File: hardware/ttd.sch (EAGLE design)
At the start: 12 parts, among them Q1 IRF540, Q2 IRF540, Q3 IRF540, Q4 IRF540

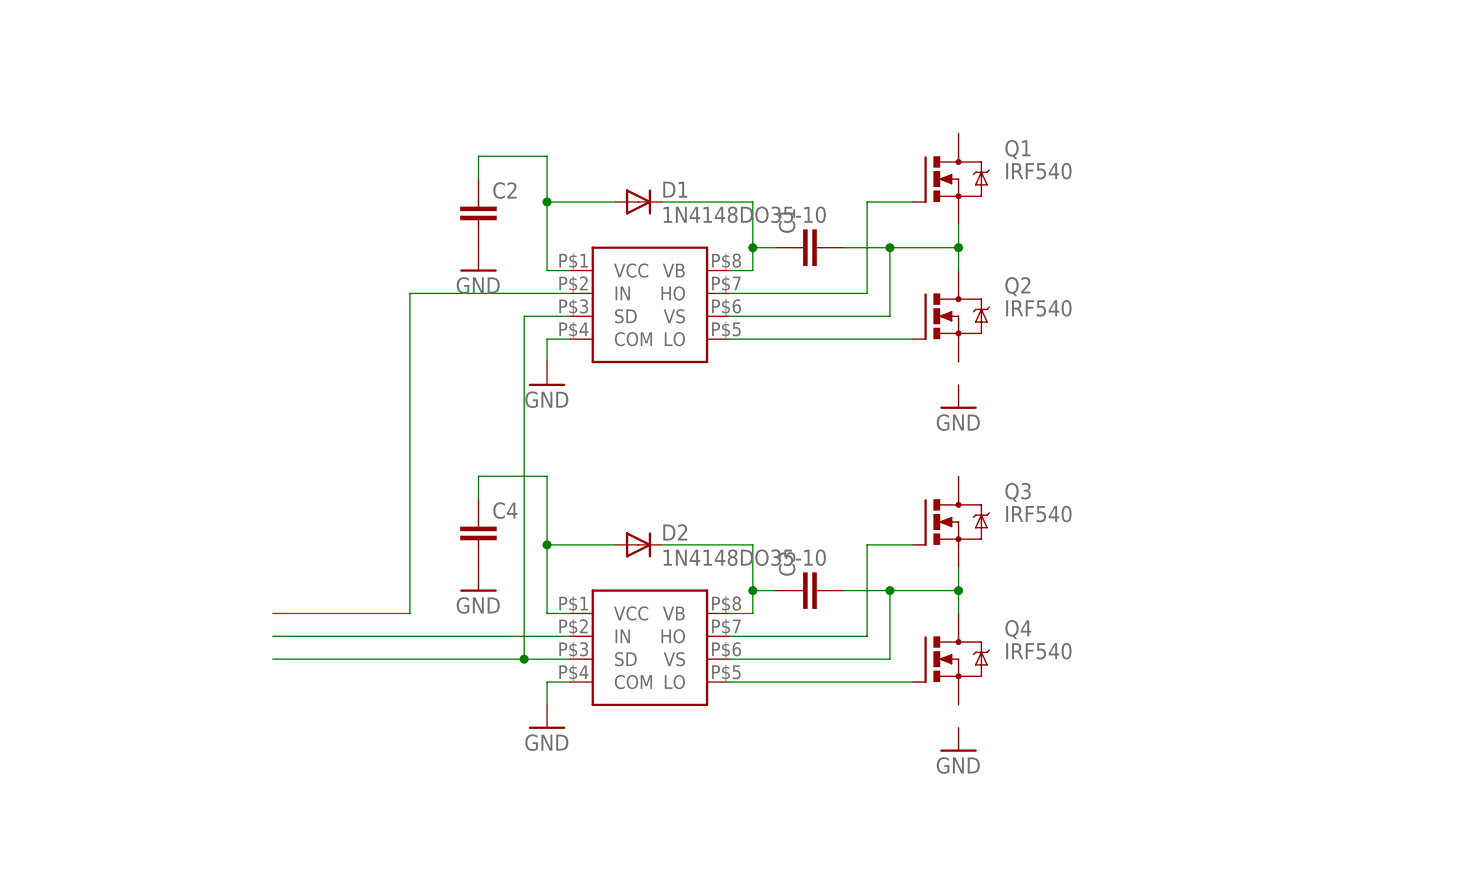
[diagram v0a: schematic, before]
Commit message: Schottkydioden eingefügt
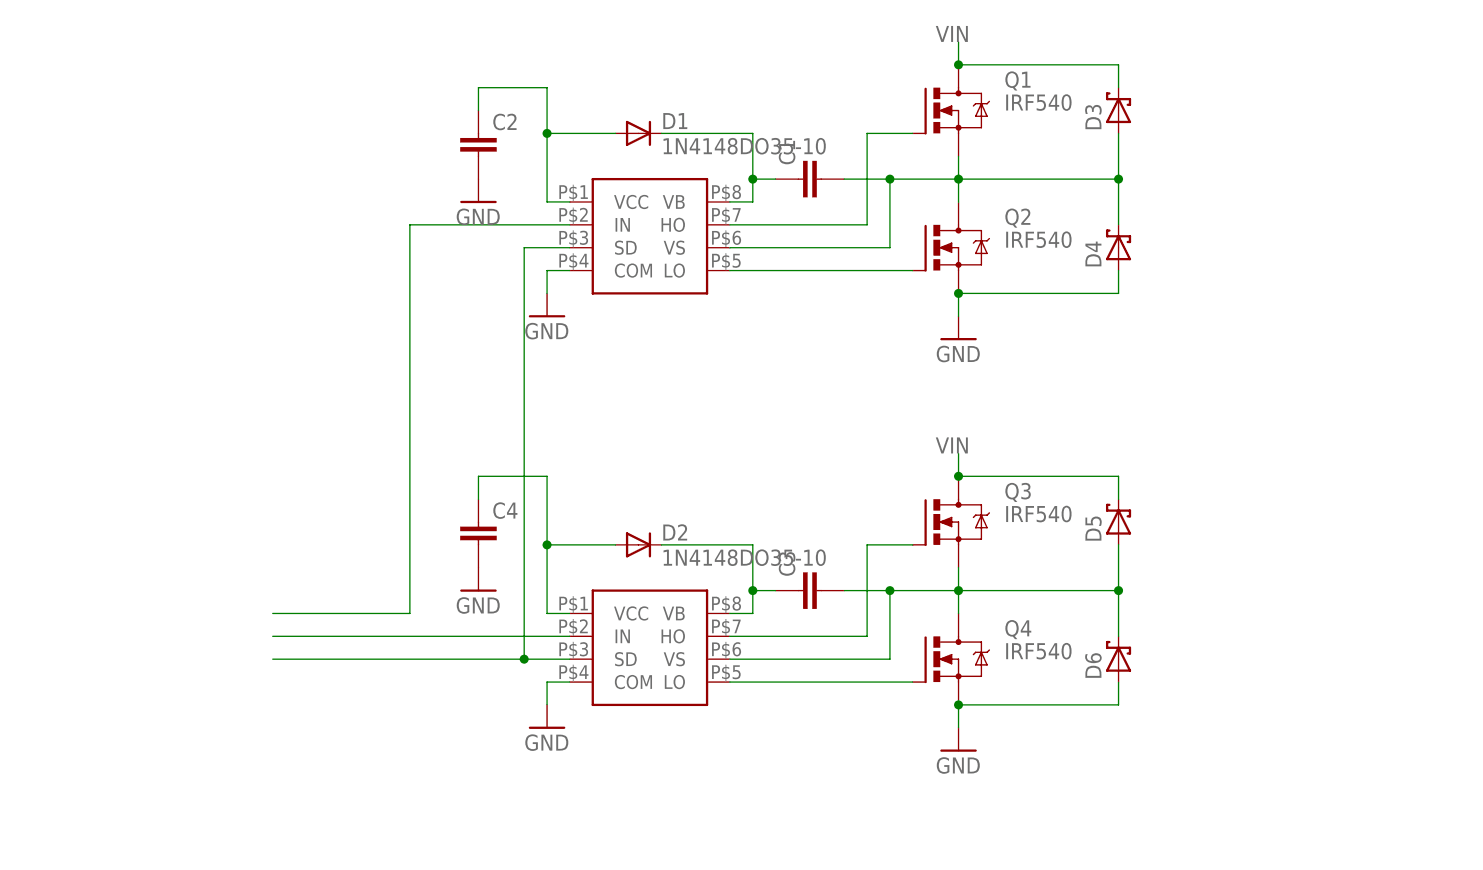
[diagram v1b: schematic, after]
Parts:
- added D3, D4, D5, D6: (no value), diode:SCHOTTKY-DIODEDO201T15
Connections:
- new net VIN: D3.C, D5.C, Q1.D, Q3.D
- net GND: now also D4.A, D6.A, Q2.S, Q4.S
- net N$4: now also D3.A, D4.C
- net N$7: now also D5.A, D6.C
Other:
- moved on the sheet: C1, C2, D1, Q1, Q2

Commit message: Stecker eingefügt
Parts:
- added X1, X2: MKDSN1,5/2-5,08, con-phoenix-508:MKDSN1,5/2-5,08
- added X3: (no value), con-phoenix-254:MPT4
- D1, D2: value 1N4148DO35-10 -> 1N4148
- D3, D4, D5, D6: value (none) -> SB540
- Q1, Q2, Q3, Q4: value IRF540 -> IRFZ44N
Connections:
- net GND: now also X2-2.KL, X3-4.1
- net N$12: now also X3-2.1, X3-3.1
- net N$15: now also X3-1.1
- net N$4: now also X1-1.KL
- net N$7: now also X1-2.KL
- net VIN: now also X2-1.KL
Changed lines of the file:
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@@
 </variantdefs>
 <classes>
-<class number="0" name="default" width="0" drill="0">
+<class number="0" name="Signal" width="0.254" drill="0">
+</class>
+<class number="1" name="Supply" width="1.27" drill="0">
+</class>
+<class number="2" name="Motor" width="1.016" drill="0">
 </class>
 </classes>
@@
 <part name="U$1" library="ttd" deviceset="IR2104" device=""/>
 <part name="U$2" library="ttd" deviceset="IR2104" device=""/>
-<part name="Q1" library="transistor-power" deviceset="IRF540" device=""/>
-<part name="Q2" library="transistor-power" deviceset="IRF540" device=""/>
-<part name="Q3" library="transistor-power" deviceset="IRF540" device=""/>
-<part name="Q4" library="transistor-power" deviceset="IRF540" device=""/>
+<part name="Q1" library="transistor-power" deviceset="IRF540" device="" value="IRFZ44N"/>
+<part name="Q2" library="transistor-power" deviceset="IRF540" device="" value="IRFZ44N"/>
+<part name="Q3" library="transistor-power" deviceset="IRF540" device="" value="IRFZ44N"/>
+<part name="Q4" library="transistor-power" deviceset="IRF540" device="" value="IRFZ44N"/>
 <part name="C1" library="rcl" deviceset="C-EU" device="050-025X075"/>
 <part name="C2" library="rcl" deviceset="C-EU" device="050-025X075"/>
 <part name="C3" library="rcl" deviceset="C-EU" device="050-025X075"/>
 <part name="C4" library="rcl" deviceset="C-EU" device="050-025X075"/>
-<part name="D1" library="diode" deviceset="1N4148" device="DO35-10"/>
-<part name="D2" library="diode" deviceset="1N4148" device="DO35-10"/>
+<part name="D1" library="diode" deviceset="1N4148" device="DO35-10" value="1N4148"/>
+<part name="D2" library="diode" deviceset="1N4148" device="DO35-10" value="1N4148"/>
 <part name="GND1" library="supply1" deviceset="GND" device=""/>
 <part name="GND2" library="supply1" deviceset="GND" device=""/>
@@
 <part name="GND5" library="supply1" deviceset="GND" device=""/>
 <part name="GND6" library="supply1" deviceset="GND" device=""/>
-<part name="D3" library="diode" deviceset="SCHOTTKY-DIODE" device="DO201T15"/>
-<part name="D4" library="diode" deviceset="SCHOTTKY-DIODE" device="DO201T15"/>
-<part name="D5" library="diode" deviceset="SCHOTTKY-DIODE" device="DO201T15"/>
-<part name="D6" library="diode" deviceset="SCHOTTKY-DIODE" device="DO201T15"/>
+<part name="D3" library="diode" deviceset="SCHOTTKY-DIODE" device="DO201T15" value="SB540"/>
+<part name="D4" library="diode" deviceset="SCHOTTKY-DIODE" device="DO201T15" value="SB540"/>
+<part name="D5" library="diode" deviceset="SCHOTTKY-DIODE" device="DO201T15" value="SB540"/>
+<part name="D6" library="diode" deviceset="SCHOTTKY-DIODE" device="DO201T15" value="SB540"/>
+<part name="X1" library="con-phoenix-508" deviceset="MKDSN1,5/2-5,08" device=""/>
+<part name="X2" library="con-phoenix-508" deviceset="MKDSN1,5/2-5,08" device=""/>
+<part name="GND7" library="supply1" deviceset="GND" device=""/>
+<part name="X3" library="con-phoenix-254" deviceset="MPT4" device=""/>
+<part name="GND8" library="supply1" deviceset="GND" device=""/>
 </parts>
 <sheets>
@@
 <instance part="D5" gate="G$1" x="106.68" y="43.18" rot="R90"/>
 <instance part="D6" gate="G$1" x="106.68" y="27.94" rot="R90"/>
+<instance part="X1" gate="-1" x="121.92" y="60.96"/>
+<instance part="X1" gate="-2" x="121.92" y="55.88"/>
+<instance part="X2" gate="-1" x="7.62" y="88.9" rot="MR0"/>
+<instance part="X2" gate="-2" x="7.62" y="83.82" rot="MR0"/>
+<instance part="GND7" gate="1" x="12.7" y="78.74"/>
+<instance part="X3" gate="-1" x="7.62" y="33.02" rot="MR0"/>
+<instance part="X3" gate="-2" x="7.62" y="30.48" rot="MR0"/>
+<instance part="X3" gate="-3" x="7.62" y="27.94" rot="MR0"/>
+<instance part="X3" gate="-4" x="7.62" y="25.4" rot="MR0"/>
+<instance part="GND8" gate="1" x="12.7" y="20.32"/>
 </instances>
 <busses>
@@
 <wire x1="106.68" y1="81.28" x2="106.68" y2="76.2" width="0.1524" layer="91"/>
 <junction x="106.68" y="81.28"/>
+<wire x1="106.68" y1="81.28" x2="114.3" y2="81.28" width="0.1524" layer="91"/>
+<wire x1="114.3" y1="81.28" x2="114.3" y2="60.96" width="0.1524" layer="91"/>
+<pinref part="X1" gate="-1" pin="KL"/>
+<wire x1="114.3" y1="60.96" x2="119.38" y2="60.96" width="0.1524" layer="91"/>
 </segment>
 </net>
@@
 <wire x1="106.68" y1="35.56" x2="106.68" y2="30.48" width="0.1524" layer="91"/>
 <junction x="106.68" y="35.56"/>
+<wire x1="106.68" y1="35.56" x2="114.3" y2="35.56" width="0.1524" layer="91"/>
+<wire x1="114.3" y1="35.56" x2="114.3" y2="55.88" width="0.1524" layer="91"/>
+<pinref part="X1" gate="-2" pin="KL"/>
+<wire x1="114.3" y1="55.88" x2="119.38" y2="55.88" width="0.1524" layer="91"/>
 </segment>
 </net>
@@
 <junction x="88.9" y="22.86"/>
 </segment>
+<segment>
+<pinref part="X2" gate="-2" pin="KL"/>
+<pinref part="GND7" gate="1" pin="GND"/>
+<wire x1="10.16" y1="83.82" x2="12.7" y2="83.82" width="0.1524" layer="91"/>
+<wire x1="12.7" y1="83.82" x2="12.7" y2="81.28" width="0.1524" layer="91"/>
+</segment>
+<segment>
+<pinref part="X3" gate="-4" pin="1"/>
+<pinref part="GND8" gate="1" pin="GND"/>
+<wire x1="10.16" y1="25.4" x2="12.7" y2="25.4" width="0.1524" layer="91"/>
+<wire x1="12.7" y1="25.4" x2="12.7" y2="22.86" width="0.1524" layer="91"/>
+</segment>
 </net>
 <net name="N$12" class="0">
@@
 <pinref part="U$2" gate="G$1" pin="IN"/>
 <wire x1="45.72" y1="30.48" x2="40.64" y2="30.48" width="0.1524" layer="91"/>
-<wire x1="12.7" y1="30.48" x2="40.64" y2="30.48" width="0.1524" layer="91"/>
+<wire x1="10.16" y1="30.48" x2="40.64" y2="30.48" width="0.1524" layer="91"/>
 <wire x1="40.64" y1="30.48" x2="40.64" y2="27.94" width="0.1524" layer="91"/>
-<wire x1="40.64" y1="27.94" x2="12.7" y2="27.94" width="0.1524" layer="91"/>
+<wire x1="40.64" y1="27.94" x2="10.16" y2="27.94" width="0.1524" layer="91"/>
 <junction x="40.64" y="27.94"/>
+<pinref part="X3" gate="-2" pin="1"/>
+<pinref part="X3" gate="-3" pin="1"/>
 </segment>
 </net>
@@
 <wire x1="45.72" y1="76.2" x2="27.94" y2="76.2" width="0.1524" layer="91"/>
 <wire x1="27.94" y1="76.2" x2="27.94" y2="33.02" width="0.1524" layer="91"/>
-<wire x1="27.94" y1="33.02" x2="12.7" y2="33.02" width="0.1524" layer="91"/>
+<wire x1="27.94" y1="33.02" x2="10.16" y2="33.02" width="0.1524" layer="91"/>
+<pinref part="X3" gate="-1" pin="1"/>
 </segment>
 </net>
@@
 <label x="86.36" y="96.52" size="1.778" layer="95"/>
 </segment>
-</net>
+<segment>
+<pinref part="X2" gate="-1" pin="KL"/>
+<wire x1="10.16" y1="88.9" x2="12.7" y2="88.9" width="0.1524" layer="91"/>
+<wire x1="12.7" y1="88.9" x2="12.7" y2="91.44" width="0.1524" layer="91"/>
+<label x="10.16" y="91.44" size="1.778" layer="95"/>
+</segment>
+</net>

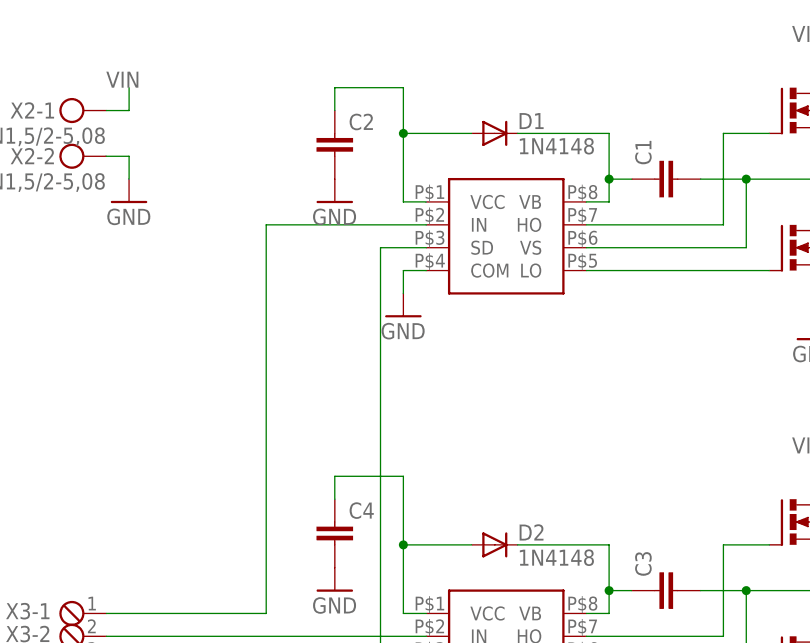
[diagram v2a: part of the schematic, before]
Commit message: Netzklassen definiert
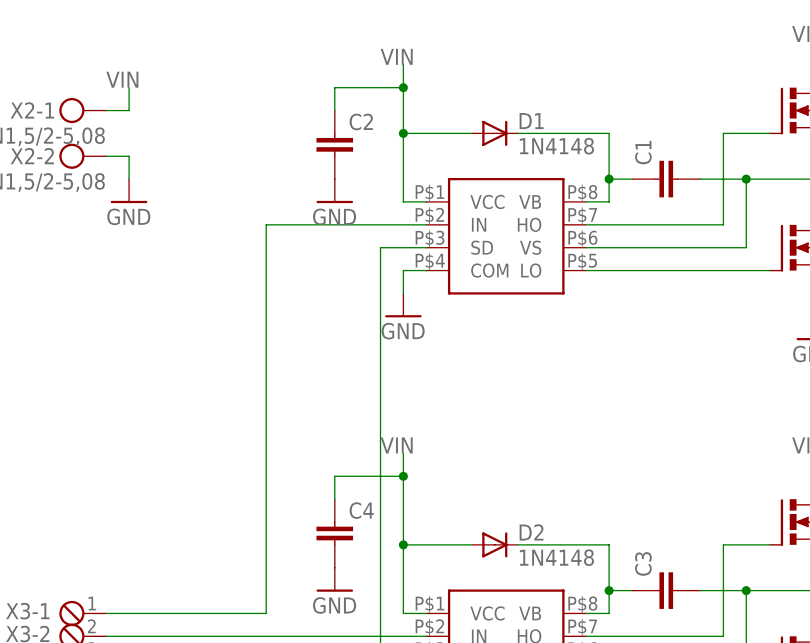
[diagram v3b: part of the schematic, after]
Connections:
- removed net N$10: C4.1, D2.A, U$2.VCC
- removed net N$11: C2.1, D1.A, U$1.VCC
- net VIN: now also C2.1, C4.1, D1.A, D2.A, U$1.VCC, U$2.VCC
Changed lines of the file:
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@@
 </segment>
 </net>
-<net name="N$4" class="0">
+<net name="N$4" class="2">
 <segment>
 <pinref part="Q1" gate="G$1" pin="S"/>
@@
 </segment>
 </net>
-<net name="N$7" class="0">
+<net name="N$7" class="2">
 <segment>
 <pinref part="C3" gate="G$1" pin="2"/>
@@
 </segment>
 </net>
-<net name="N$10" class="0">
-<segment>
-<pinref part="D2" gate="G$1" pin="A"/>
-<wire x1="50.8" y1="40.64" x2="43.18" y2="40.64" width="0.1524" layer="91"/>
-<wire x1="43.18" y1="40.64" x2="43.18" y2="33.02" width="0.1524" layer="91"/>
-<pinref part="U$2" gate="G$1" pin="VCC"/>
-<wire x1="43.18" y1="33.02" x2="45.72" y2="33.02" width="0.1524" layer="91"/>
-<pinref part="C4" gate="G$1" pin="1"/>
-<wire x1="35.56" y1="45.72" x2="35.56" y2="48.26" width="0.1524" layer="91"/>
-<wire x1="35.56" y1="48.26" x2="43.18" y2="48.26" width="0.1524" layer="91"/>
-<wire x1="43.18" y1="48.26" x2="43.18" y2="40.64" width="0.1524" layer="91"/>
-<junction x="43.18" y="40.64"/>
-</segment>
-</net>
-<net name="N$11" class="0">
-<segment>
-<pinref part="D1" gate="G$1" pin="A"/>
-<wire x1="50.8" y1="86.36" x2="43.18" y2="86.36" width="0.1524" layer="91"/>
-<wire x1="43.18" y1="86.36" x2="43.18" y2="78.74" width="0.1524" layer="91"/>
-<pinref part="U$1" gate="G$1" pin="VCC"/>
-<wire x1="43.18" y1="78.74" x2="45.72" y2="78.74" width="0.1524" layer="91"/>
-<pinref part="C2" gate="G$1" pin="1"/>
-<wire x1="35.56" y1="88.9" x2="35.56" y2="91.44" width="0.1524" layer="91"/>
-<wire x1="35.56" y1="91.44" x2="43.18" y2="91.44" width="0.1524" layer="91"/>
-<wire x1="43.18" y1="91.44" x2="43.18" y2="86.36" width="0.1524" layer="91"/>
-<junction x="43.18" y="86.36"/>
-</segment>
-</net>
-<net name="GND" class="0">
+<net name="GND" class="1">
 <segment>
 <pinref part="C4" gate="G$1" pin="2"/>
@@
 </segment>
 </net>
-<net name="VIN" class="0">
+<net name="VIN" class="1">
 <segment>
 <pinref part="D5" gate="G$1" pin="C"/>
@@
 <label x="10.16" y="91.44" size="1.778" layer="95"/>
 </segment>
-</net>
+<segment>
+<pinref part="D2" gate="G$1" pin="A"/>
+<wire x1="50.8" y1="40.64" x2="43.18" y2="40.64" width="0.1524" layer="91"/>
+<wire x1="43.18" y1="40.64" x2="43.18" y2="33.02" width="0.1524" layer="91"/>
+<pinref part="U$2" gate="G$1" pin="VCC"/>
+<wire x1="43.18" y1="33.02" x2="45.72" y2="33.02" width="0.1524" layer="91"/>
+<pinref part="C4" gate="G$1" pin="1"/>
+<wire x1="35.56" y1="45.72" x2="35.56" y2="48.26" width="0.1524" layer="91"/>
+<wire x1="35.56" y1="48.26" x2="43.18" y2="48.26" width="0.1524" layer="91"/>
+<wire x1="43.18" y1="48.26" x2="43.18" y2="40.64" width="0.1524" layer="91"/>
+<junction x="43.18" y="40.64"/>
+<wire x1="43.18" y1="48.26" x2="43.18" y2="50.8" width="0.1524" layer="91"/>
+<junction x="43.18" y="48.26"/>
+<label x="40.64" y="50.8" size="1.778" layer="95"/>
+</segment>
+<segment>
+<pinref part="D1" gate="G$1" pin="A"/>
+<wire x1="50.8" y1="86.36" x2="43.18" y2="86.36" width="0.1524" layer="91"/>
+<wire x1="43.18" y1="86.36" x2="43.18" y2="78.74" width="0.1524" layer="91"/>
+<pinref part="U$1" gate="G$1" pin="VCC"/>
+<wire x1="43.18" y1="78.74" x2="45.72" y2="78.74" width="0.1524" layer="91"/>
+<pinref part="C2" gate="G$1" pin="1"/>
+<wire x1="35.56" y1="88.9" x2="35.56" y2="91.44" width="0.1524" layer="91"/>
+<wire x1="35.56" y1="91.44" x2="43.18" y2="91.44" width="0.1524" layer="91"/>
+<wire x1="43.18" y1="91.44" x2="43.18" y2="86.36" width="0.1524" layer="91"/>
+<junction x="43.18" y="86.36"/>
+<wire x1="43.18" y1="91.44" x2="43.18" y2="93.98" width="0.1524" layer="91"/>
+<junction x="43.18" y="91.44"/>
+<label x="40.64" y="93.98" size="1.778" layer="95"/>
+</segment>
+</net>

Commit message: Layout
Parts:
- C2, C4: device rcl:C-EU050-025X075 -> resistor:C-EU075-032X103
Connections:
- net N$15 renamed A
- removed net N$12: U$1.SD, U$2.IN, U$2.SD, X3-2.1, X3-3.1
- new net B: U$2.IN, X3-2.1
- new net PWM: U$1.SD, U$2.SD, X3-3.1
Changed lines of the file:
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@@
 <part name="Q4" library="transistor-power" deviceset="IRF540" device="" value="IRFZ44N"/>
 <part name="C1" library="rcl" deviceset="C-EU" device="050-025X075"/>
-<part name="C2" library="rcl" deviceset="C-EU" device="050-025X075"/>
+<part name="C2" library="resistor" deviceset="C-EU" device="075-032X103"/>
 <part name="C3" library="rcl" deviceset="C-EU" device="050-025X075"/>
-<part name="C4" library="rcl" deviceset="C-EU" device="050-025X075"/>
+<part name="C4" library="resistor" deviceset="C-EU" device="075-032X103"/>
 <part name="D1" library="diode" deviceset="1N4148" device="DO35-10" value="1N4148"/>
 <part name="D2" library="diode" deviceset="1N4148" device="DO35-10" value="1N4148"/>
@@
 </segment>
 </net>
-<net name="N$12" class="0">
+<net name="PWM" class="0">
 <segment>
 <pinref part="U$1" gate="G$1" pin="SD"/>
 <wire x1="45.72" y1="73.66" x2="40.64" y2="73.66" width="0.1524" layer="91"/>
-<wire x1="40.64" y1="73.66" x2="40.64" y2="30.48" width="0.1524" layer="91"/>
+<wire x1="40.64" y1="73.66" x2="40.64" y2="27.94" width="0.1524" layer="91"/>
 <pinref part="U$2" gate="G$1" pin="SD"/>
 <wire x1="40.64" y1="27.94" x2="45.72" y2="27.94" width="0.1524" layer="91"/>
-<pinref part="U$2" gate="G$1" pin="IN"/>
-<wire x1="45.72" y1="30.48" x2="40.64" y2="30.48" width="0.1524" layer="91"/>
-<wire x1="10.16" y1="30.48" x2="40.64" y2="30.48" width="0.1524" layer="91"/>
-<wire x1="40.64" y1="30.48" x2="40.64" y2="27.94" width="0.1524" layer="91"/>
 <wire x1="40.64" y1="27.94" x2="10.16" y2="27.94" width="0.1524" layer="91"/>
 <junction x="40.64" y="27.94"/>
-<pinref part="X3" gate="-2" pin="1"/>
 <pinref part="X3" gate="-3" pin="1"/>
-</segment>
-</net>
-<net name="N$15" class="0">
+<label x="12.7" y="27.94" size="1.778" layer="95"/>
+</segment>
+</net>
+<net name="A" class="0">
 <segment>
 <pinref part="U$1" gate="G$1" pin="IN"/>
@@
 <wire x1="27.94" y1="33.02" x2="10.16" y2="33.02" width="0.1524" layer="91"/>
 <pinref part="X3" gate="-1" pin="1"/>
+<label x="12.7" y="33.02" size="1.778" layer="95"/>
 </segment>
 </net>
@@
 </segment>
 </net>
+<net name="B" class="2">
+<segment>
+<pinref part="X3" gate="-2" pin="1"/>
+<pinref part="U$2" gate="G$1" pin="IN"/>
+<wire x1="10.16" y1="30.48" x2="45.72" y2="30.48" width="0.1524" layer="91"/>
+<label x="12.7" y="30.48" size="1.778" layer="95"/>
+</segment>
+</net>
